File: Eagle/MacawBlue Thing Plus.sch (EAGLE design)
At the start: 66 parts, among them J2 CORTEX_DEBUG, J5 USB-C, J8 U.FL, U1 MCP73831, U2 3.3V, U3 NM180100, U4 CH340E_MSOP10, U5 3.3V, U6 DPX202700DT-4162A1, Y1 32.768kHz

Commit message: Added 4-layer board
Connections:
- net ~D19/A0: now also U3.GPIO13; no longer U3.GPIO12
- net ~D20/A1: now also U3.GPIO12; no longer U3.GPIO13
- net ~D22/A3: now also U3.GPIO33; no longer U3.GPIO29
- net ~D23/A4: now also U3.GPIO34; no longer U3.GPIO11
- net ~D24/A5: now also U3.GPIO11; no longer U3.GPIO33
- net ~D5: now also U3.GPIO30; no longer U3.GPIO24
- net ~D6: now also U3.GPIO37; no longer U3.GPIO30
- net ~D7: now also U3.GPIO24; no longer U3.GPIO37
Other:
- note added: "MacawBlue (Apollo3)"
- note removed: "Artemis (Apollo3)"
- moved on the sheet: D7, R12, S2

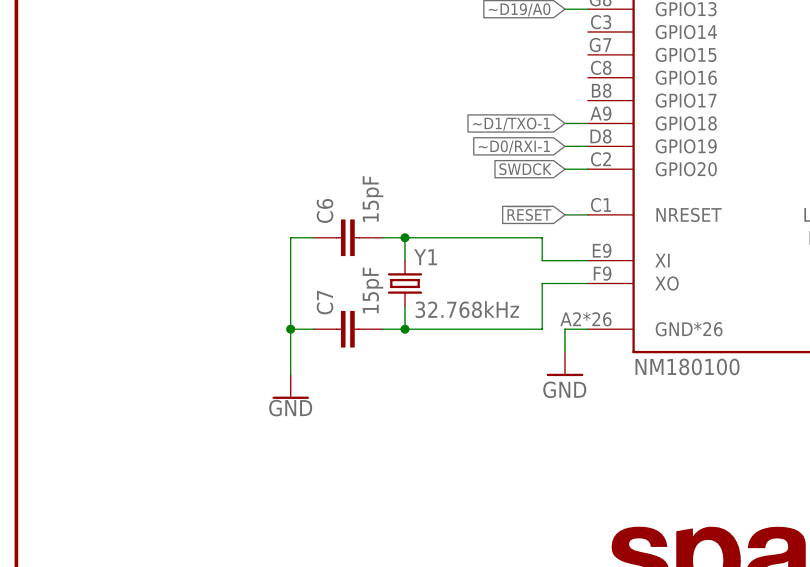
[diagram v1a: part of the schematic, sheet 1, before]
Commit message: Fixed NM180100 footprint
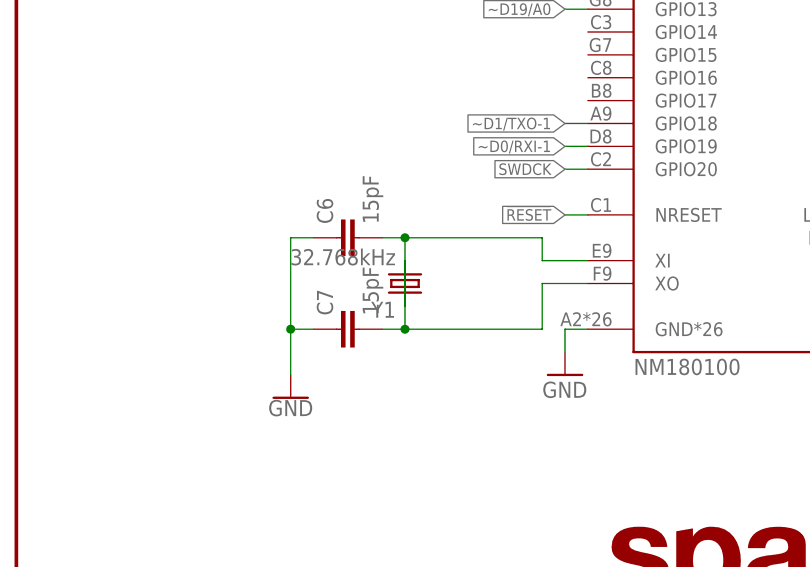
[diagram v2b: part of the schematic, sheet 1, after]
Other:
- note added: "LoRa Regulator"
- note removed: "Lora Regualtor"
- moved on the sheet: Y1
